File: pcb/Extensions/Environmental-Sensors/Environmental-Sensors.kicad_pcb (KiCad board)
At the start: 2 copper layers, 20.2 x 18 mm, 18 parts, among them J1 Conn_01x04, U1 CCS811, U2 ENS210, U3 BMP280

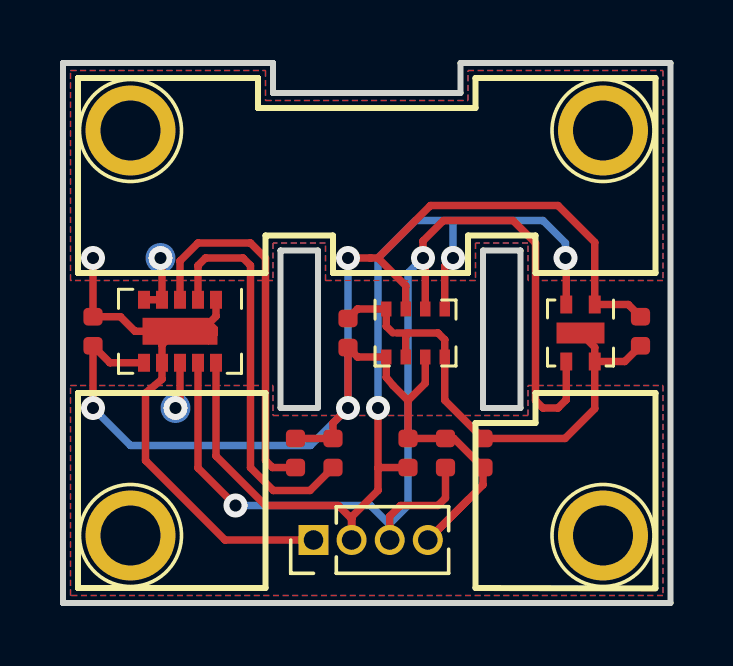
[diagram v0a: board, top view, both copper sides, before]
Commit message: Upgrade Environmental Sensors to KiCad 6.0
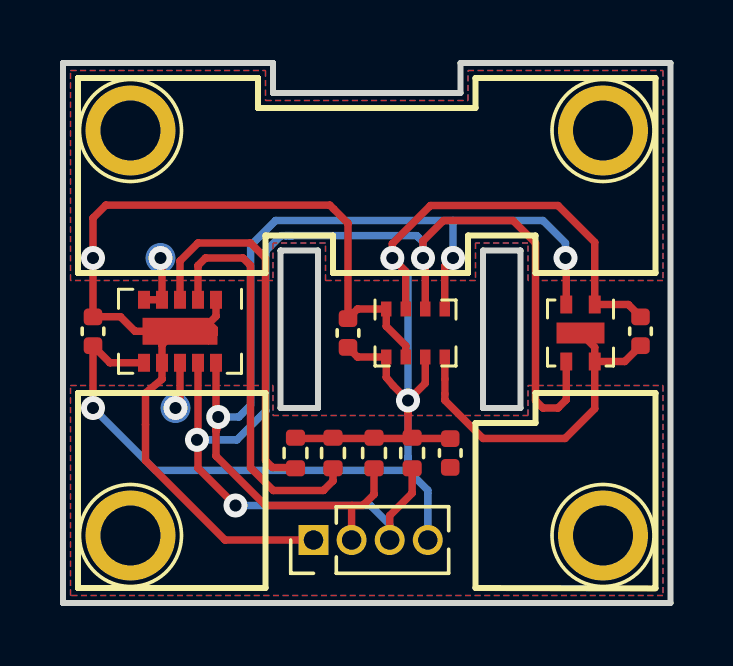
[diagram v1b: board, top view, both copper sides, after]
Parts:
- added NT1: NetTie_2, NetTie:NetTie-2_SMD_Pad0.25mm, F.Cu at (121.0, 81.5)
- moved R2 1.13 mm to (118.6, 83.8)
- moved R1 1.11 mm to (119.9, 83.8)
- moved C2 1.09 mm to (121.2, 83.8), turned to -90 degrees
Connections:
- U3 pad 5: GND -> Net-(NT1-Pad2)
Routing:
- net GND: track 37.3 -> 46.2 mm
- net /SDA: track 40.1 -> 42.9 mm, vias 2 -> 3
- net /SCL: track 32.3 -> 34.6 mm
- net +3V3: track 52.6 -> 50.4 mm
- net Net-(NT1-Pad2): track 0.00 -> 0.73 mm
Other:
- net class Default removed
- board text added: "BasilFX 09/2022 V1.3.0"
- board text removed: "BasilFX 08/2018 V1.2.0"
